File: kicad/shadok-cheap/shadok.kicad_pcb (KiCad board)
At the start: 2 copper layers, 141.2 x 57.8 mm, 123 parts, among them J101 TEST_1P, J103 TEST_1P, J104 TEST_1P, J105 SERIALS, J401 Conn_02x05_Odd_Even, J501 Micro_SD_Card, J502 TEST_1P, J601 74LVC8T245, J602 74LVC8T245, J603 74LVC8T245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

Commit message: waveforms
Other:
- board text added: "SVO 2018"
- board text removed: "SVO 2008"
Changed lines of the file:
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@@
   )
   (setup
-    (last_trace_width 1)
+    (last_trace_width 0.16)
     (user_trace_width 0.3)
     (user_trace_width 0.4)
@@
     (tags "capacitor 0603")
     (attr smd)
-    (fp_text reference C205 (at 0 -1.5 90) (layer F.SilkS)
+    (fp_text reference C205 (at -0.254 1.143 90) (layer F.SilkS)
       (effects (font (size 0.6 0.6) (thickness 0.15)))
     )
@@
     (tags "capacitor 0805")
     (attr smd)
-    (fp_text reference C207 (at 0 -1.5 180) (layer F.SilkS)
+    (fp_text reference C207 (at 3.048 0 180) (layer F.SilkS)
       (effects (font (size 0.6 0.6) (thickness 0.15)))
     )
@@
     (tags SOT-23-5)
     (attr smd)
-    (fp_text reference U202 (at 0 -2.9) (layer F.SilkS)
+    (fp_text reference U202 (at -0.127 1.905) (layer F.SilkS)
       (effects (font (size 0.6 0.6) (thickness 0.15)))
     )
@@
     (effects (font (size 1 1.5) (thickness 0.25)))
   )
-  (gr_text "SVO 2008" (at 160.3375 165.1 315) (layer F.SilkS)
+  (gr_text "SVO 2018" (at 160.3375 165.1 315) (layer F.SilkS)
     (effects (font (size 1 0.8) (thickness 0.15)) (justify right))
   )

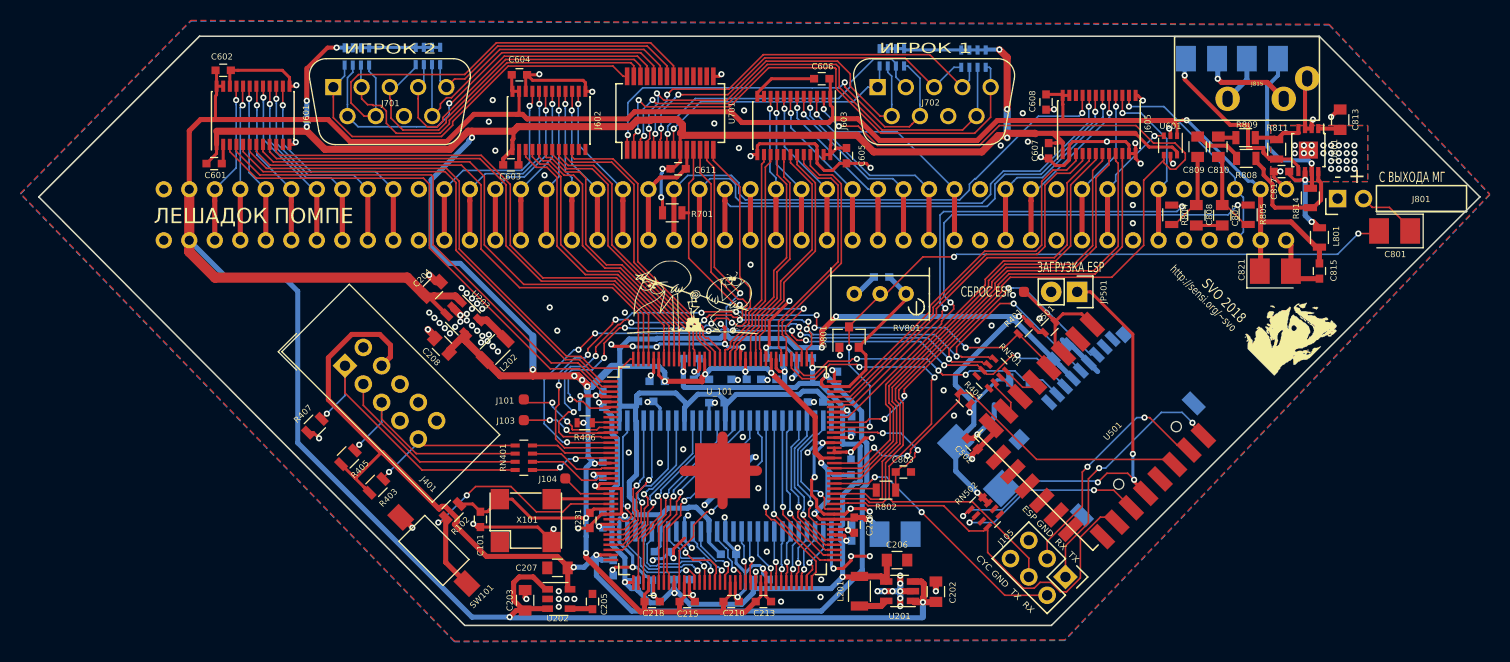
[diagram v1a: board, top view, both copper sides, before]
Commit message: first working version
kvaz in sdram
AY emulation
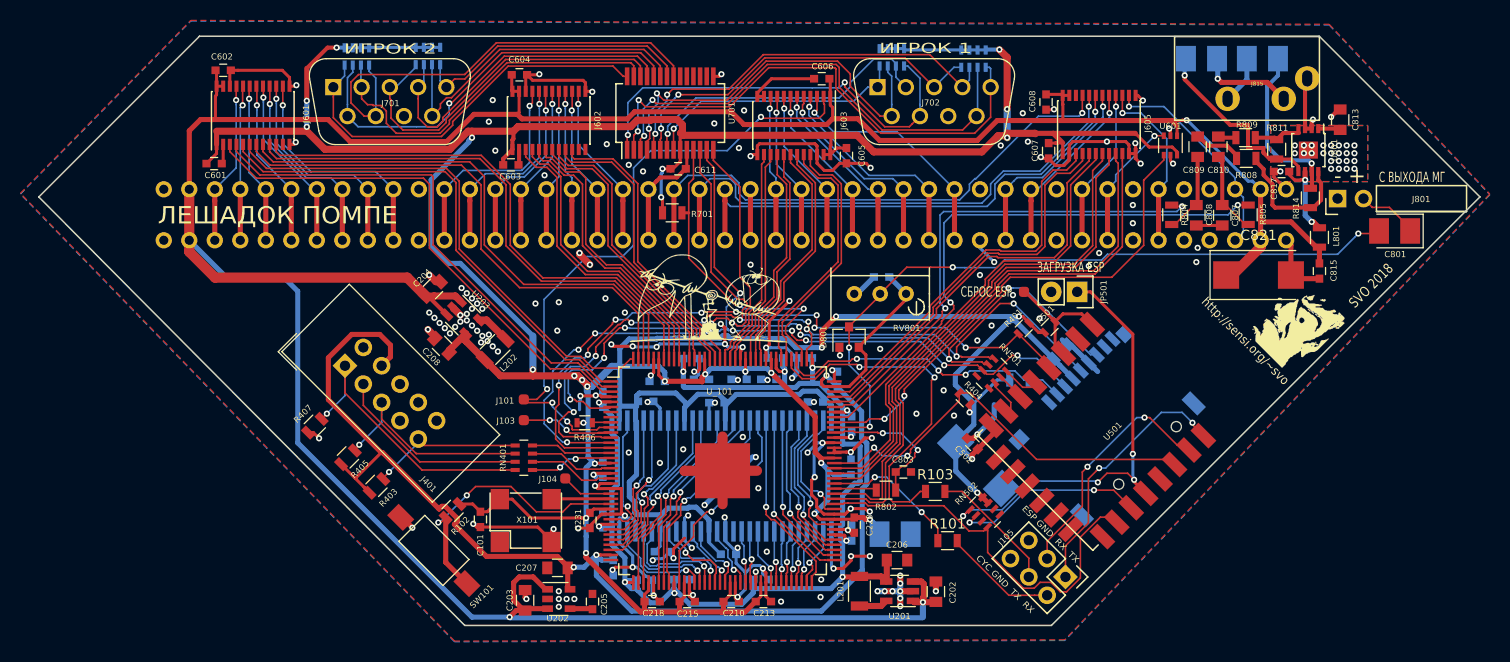
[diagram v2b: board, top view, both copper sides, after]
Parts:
- removed the G*** at (106.4, 162.6)
- added G***: LOGO, shadki:pompaient9mm, F.Cu at (108.0, 162.7)
- added R101: 100, Resistors_SMD:R_0805, F.Cu at (131.3, 186.7)
- added R103: 100, Resistors_SMD:R_0805, F.Cu at (130.1, 181.9)
- C820, C822: value 68.0 -> 47.0
- C821: value 68.0 -> 47.0; footprint Capacitors_Tantalum_SMD:CP_Tantalum_Case-B_EIA-3528-21_Reflow -> Capacitors_Tantalum_SMD:CP_Tantalum_Case-D_EIA-7343-31_Reflow
- L801: value LQH66SN101M 100uH -> BLM21AG102SN1D
- moved C821 1.69 mm to (161.8, 160.7)
- moved G*** 1.08 mm to (165.0, 165.1)
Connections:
- J101 pad 1: /FREE_IO1 -> /~DDIR
- J105 pad 2: /ESP_RxD -> Net-(J105-Pad2)
- J105 pad 4: /ESP_TxD -> Net-(J105-Pad4)
- J603 pad 2: /~БЛК -> /~DDIR
- U_101 pad 10: /FREE_IO1 -> /~DDIR
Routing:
- net /~DDIR: track 0.00 -> 63.1 mm, vias 0 -> 4
- net /~БЛК: track 92.0 -> 48.1 mm, vias 4 -> 2
- net /ESP_TxD: track 48.1 -> 34.3 mm
- net Net-(J105-Pad4): track 0.00 -> 12.8 mm
- net /ESP_RxD: track 25.9 -> 13.7 mm
- net Net-(J105-Pad2): track 0.00 -> 11.2 mm
- net /FREE_IO1: track 10.3 -> 0.00 mm, vias 2 -> 0
- net GND: track 308.1 -> 312.4 mm, vias 146 -> 160
- net +5V: track 307.6 -> 310.1 mm

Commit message: sdram arbitre for zpu or anything really WIP
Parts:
- added Q601: BC817, TO_SOT_Packages_SMD:SOT-23, F.Cu at (146.4, 140.0)
- added R601: 10K, Resistors_SMD:R_0805, F.Cu at (150.8, 140.2)
- added R602: 10K, Resistors_SMD:R_0805, F.Cu at (141.9, 140.0)
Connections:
- net /FREE_I1 renamed /СБРОС
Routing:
- net /СБРОС: track 5.08 -> 107.7 mm, vias 0 -> 2
- net /BUS/~СБРОСЪ: track 0.00 -> 14.4 mm
- net Net-(Q601-Pad1): track 0.00 -> 5.09 mm
- net +3V3: track 500.0 -> 503.8 mm
- net /~DDIR: track 63.1 -> 60.8 mm
- net GND: track 312.4 -> 314.1 mm, vias 160 -> 173

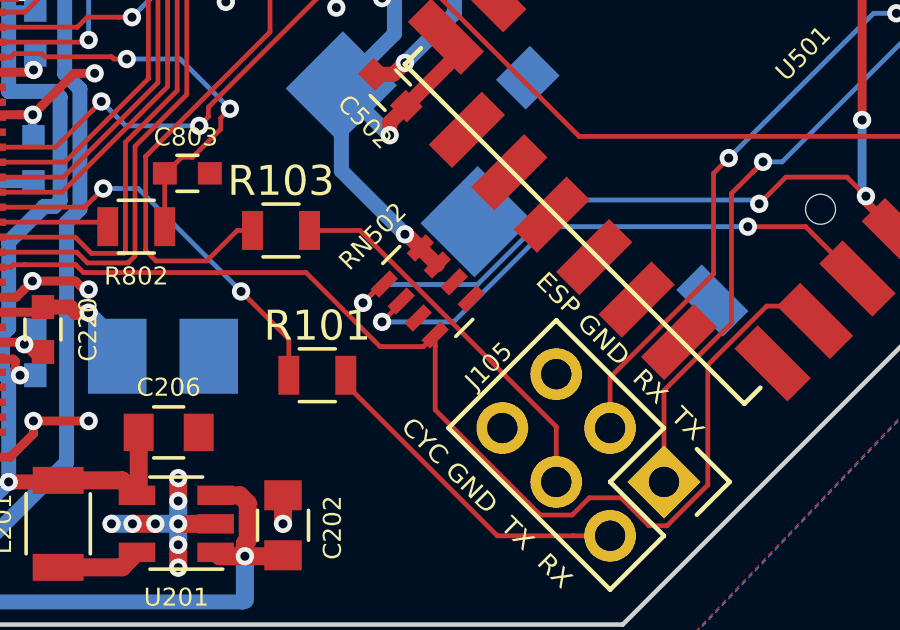
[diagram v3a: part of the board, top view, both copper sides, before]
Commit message: documented bodge pulldown R502 across RN502
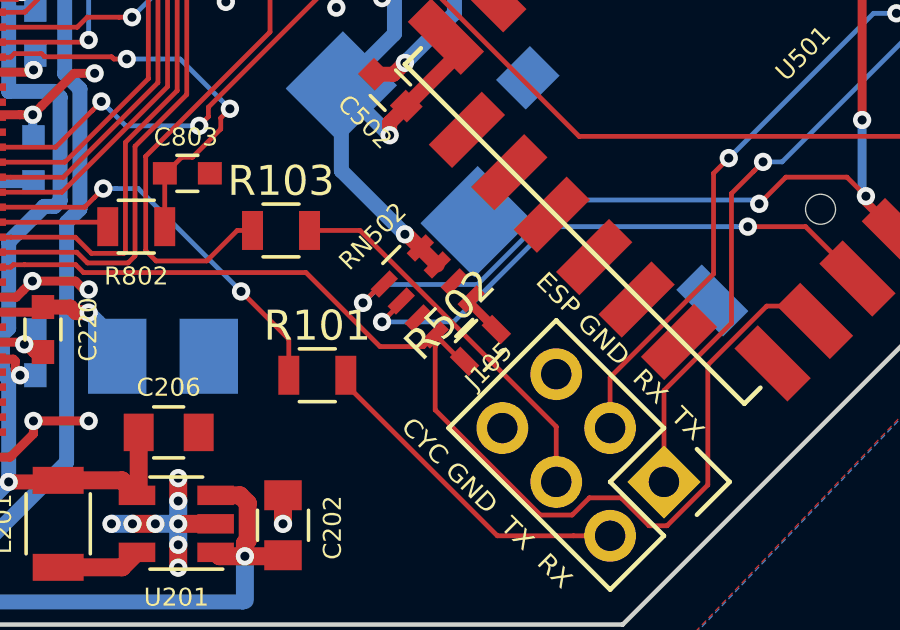
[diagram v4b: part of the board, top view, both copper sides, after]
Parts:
- added R502: 4K7, Resistors_SMD:R_0603, F.Cu at (136.8, 185.7)
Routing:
- net GND: track 314.1 -> 315.5 mm
- net /~ESP_SS: track 38.5 -> 39.8 mm
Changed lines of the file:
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@@
     (thickness 1.6)
     (drawings 19)
-    (tracks 3279)
+    (tracks 3283)
     (zones 0)
-    (modules 128)
+    (modules 129)
     (nets 215)
   )
@@
     )
   )
+  (module Resistors_SMD:R_0603 (layer F.Cu)
+    (at 136.75667 185.69633 45)
+    (descr "Resistor SMD 0603, reflow soldering, Vishay (see dcrcw.pdf)")
+    (tags "resistor 0603")
+    (attr smd)
+    (fp_text reference R502 (at 0 -1.45 45) (layer F.SilkS)
+      (effects (font (size 1 1) (thickness 0.15)))
+    )
+    (fp_text value 4K7 (at 0 1.5 45) (layer F.Fab)
+      (effects (font (size 1 1) (thickness 0.15)))
+    )
+    (fp_text user %R (at 0 0 45) (layer F.Fab)
+      (effects (font (size 0.4 0.4) (thickness 0.075)))
+    )
+    (fp_line (start -0.8 0.4) (end -0.8 -0.4) (layer F.Fab) (width 0.1))
+    (fp_line (start 0.8 0.4) (end -0.8 0.4) (layer F.Fab) (width 0.1))
+    (fp_line (start 0.8 -0.4) (end 0.8 0.4) (layer F.Fab) (width 0.1))
+    (fp_line (start -0.8 -0.4) (end 0.8 -0.4) (layer F.Fab) (width 0.1))
+    (fp_line (start 0.5 0.68) (end -0.5 0.68) (layer F.SilkS) (width 0.12))
+    (fp_line (start -0.5 -0.68) (end 0.5 -0.68) (layer F.SilkS) (width 0.12))
+    (fp_line (start -1.25 -0.7) (end 1.25 -0.7) (layer F.CrtYd) (width 0.05))
+    (fp_line (start -1.25 -0.7) (end -1.25 0.7) (layer F.CrtYd) (width 0.05))
+    (fp_line (start 1.25 0.7) (end 1.25 -0.7) (layer F.CrtYd) (width 0.05))
+    (fp_line (start 1.25 0.7) (end -1.25 0.7) (layer F.CrtYd) (width 0.05))
+    (pad 1 smd rect (at -0.75 0 45) (size 0.5 0.9) (layers F.Cu F.Paste F.Mask)
+      (net 165 /~ESP_SS))
+    (pad 2 smd rect (at 0.75 0 45) (size 0.5 0.9) (layers F.Cu F.Paste F.Mask)
+      (net 2 GND))
+    (model ${KISYS3DMOD}/Resistors_SMD.3dshapes/R_0603.wrl
+      (at (xyz 0 0 0))
+      (scale (xyz 1 1 1))
+      (rotate (xyz 0 0 0))
+    )
+  )
   (gr_text "ИГРОК 1" (at 129.159 138.43) (layer F.SilkS)
     (effects (font (size 1 1.5) (thickness 0.25)))
@@
   (segment (start 89.154 144.907) (end 89.325 144.736) (width 0.3) (layer F.Cu) (net 1))
   (segment (start 89.325 144.736) (end 89.325 142.65) (width 0.3) (layer F.Cu) (net 1) (status 20))
+  (segment (start 136.450569 184.143487) (end 136.450569 184.329569) (width 0.3) (layer F.Cu) (net 2))
+  (segment (start 136.450569 184.329569) (end 137.287 185.166) (width 0.3) (layer F.Cu) (net 2))
   (via (at 138.303 138.938) (size 0.61) (drill 0.3) (layers F.Cu B.Cu) (net 2))
   (via (at 136.144 140.081) (size 0.61) (drill 0.3) (layers F.Cu B.Cu) (net 2))
@@
   (segment (start 104.784817 146.007018) (end 104.479818 146.312017) (width 0.16) (layer B.Cu) (net 109))
   (segment (start 122.121767 143.618233) (end 107.173602 143.618233) (width 0.16) (layer B.Cu) (net 109))
+  (segment (start 136.22634 186.22666) (end 136.129578 186.22666) (width 0.16) (layer F.Cu) (net 165))
+  (segment (start 136.129578 186.22666) (end 135.248487 185.345569) (width 0.16) (layer F.Cu) (net 165))
   (segment (start 125.943996 182.88) (end 127.633 182.88) (width 0.16) (layer F.Cu) (net 166))
   (segment (start 127.633 182.88) (end 128.649 181.864) (width 0.16) (layer F.Cu) (net 166))

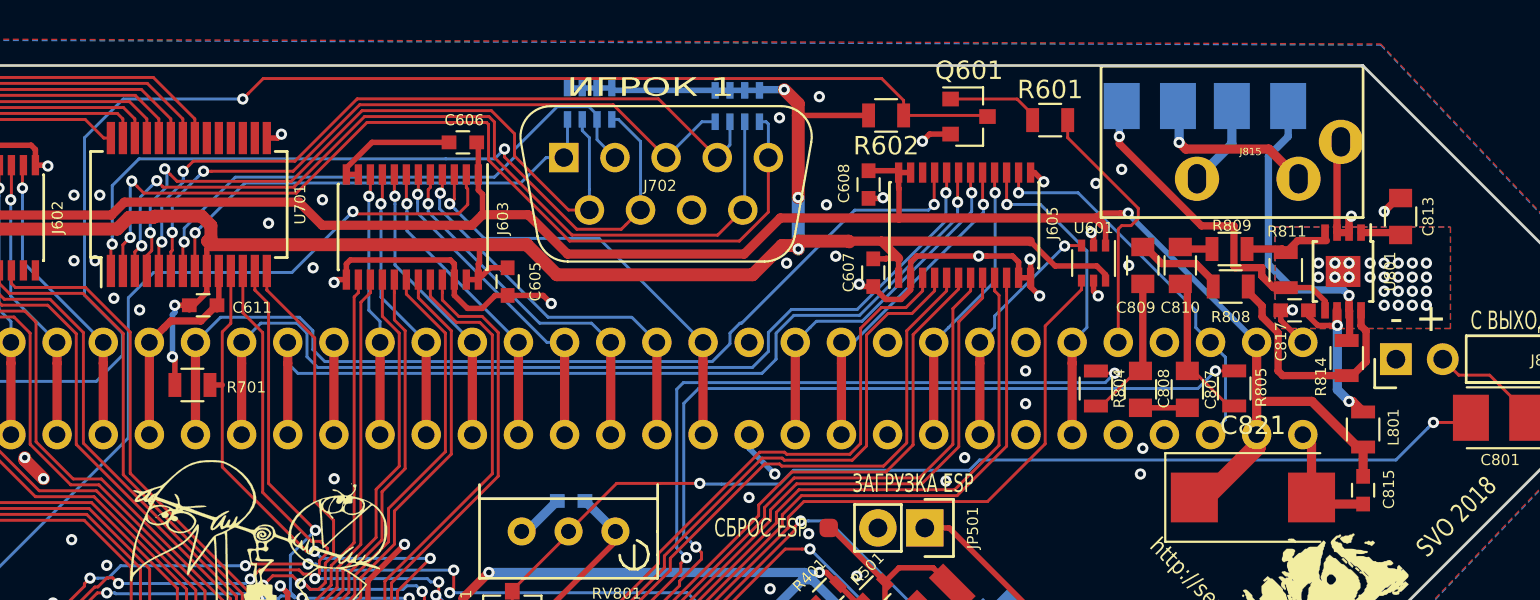
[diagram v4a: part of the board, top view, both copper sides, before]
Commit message: joystick "C" on ports 2e/2f works well
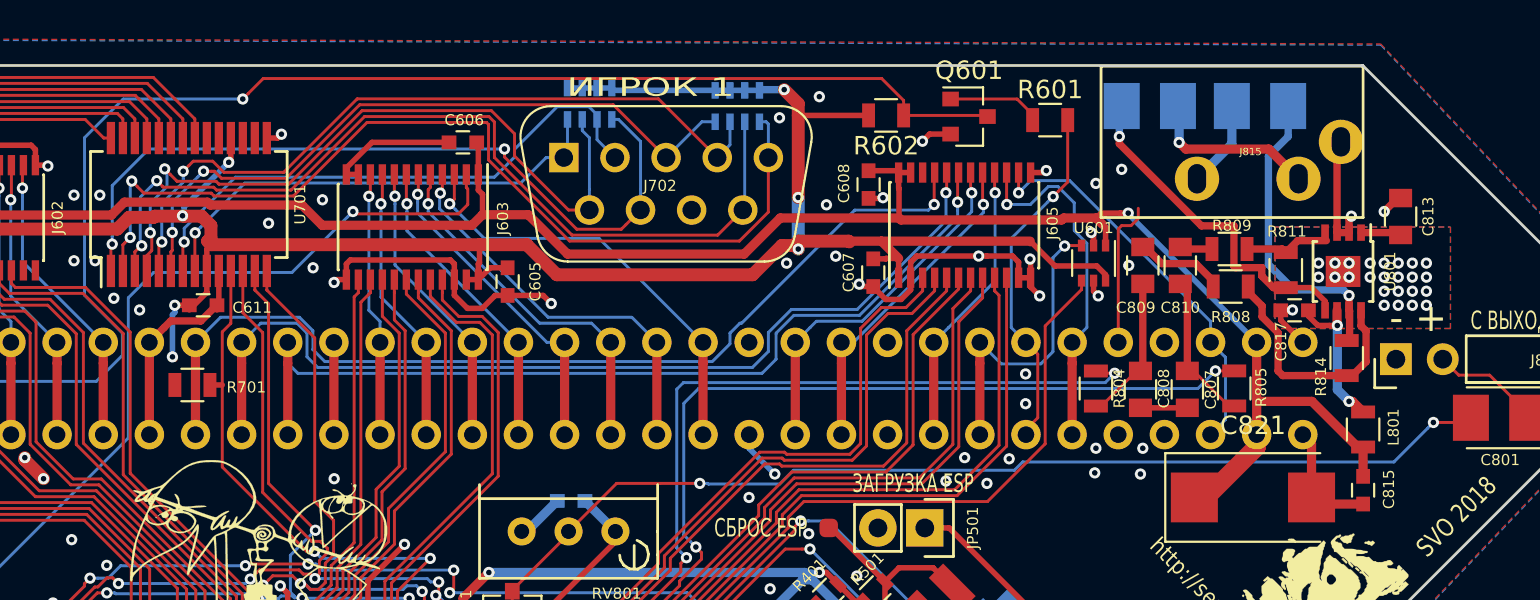
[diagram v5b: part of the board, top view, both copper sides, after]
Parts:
- RN502: value 10K -> 3K3
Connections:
- J604 pad 39: Net-(J604-Pad39) -> /BUS/~ВВОДЪ_СИСТЕМЫ
- R601 pad 2: /BUS/~СБРОСЪ -> /BUS/~ВВОДЪ_СИСТЕМЫ
- R701 pad 2: +3V3 -> Net-(R701-Pad2)
- U701 pad 18: GND -> +3V3
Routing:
- net /BUS/~ВВОДЪ_СИСТЕМЫ: track 0.00 -> 19.2 mm, vias 0 -> 1
- net /BUS/~СБРОСЪ: track 14.4 -> 8.01 mm
- net +3V3: track 503.8 -> 507.7 mm, vias 30 -> 32
- net /BUS/~БЛКЪ: track 13.1 -> 16.6 mm
- net /BUS/СТЕКЪ: track 17.4 -> 19.3 mm
- net /BUS/СТРОБЪ_СОСТЪ: track 21.1 -> 21.7 mm
- net /Joysticks/~P1RT: track 40.1 -> 40.6 mm
- net GND: track 315.5 -> 315.4 mm, vias 173 -> 177
